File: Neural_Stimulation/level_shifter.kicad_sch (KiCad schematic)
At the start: 4 parts, among them U6 SN74LV1T34DBV, U7 SN74LV1T34DBV, U8 SN74LV1T34DBV, U9 SN74LV1T34DBV

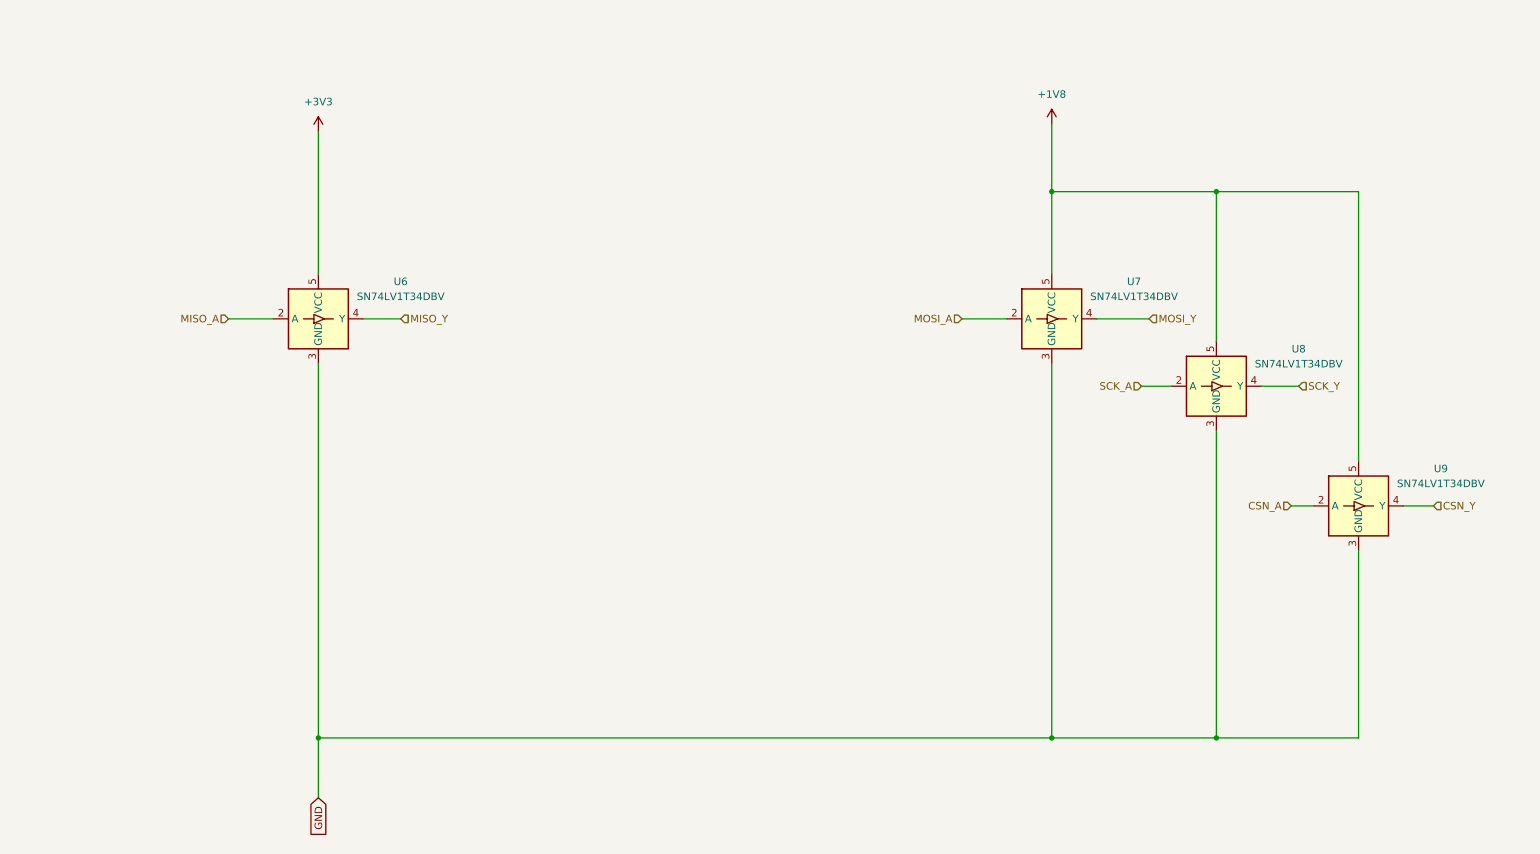
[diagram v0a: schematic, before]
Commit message: Added INT, TRIG, ATEST and RSTN pin circuits
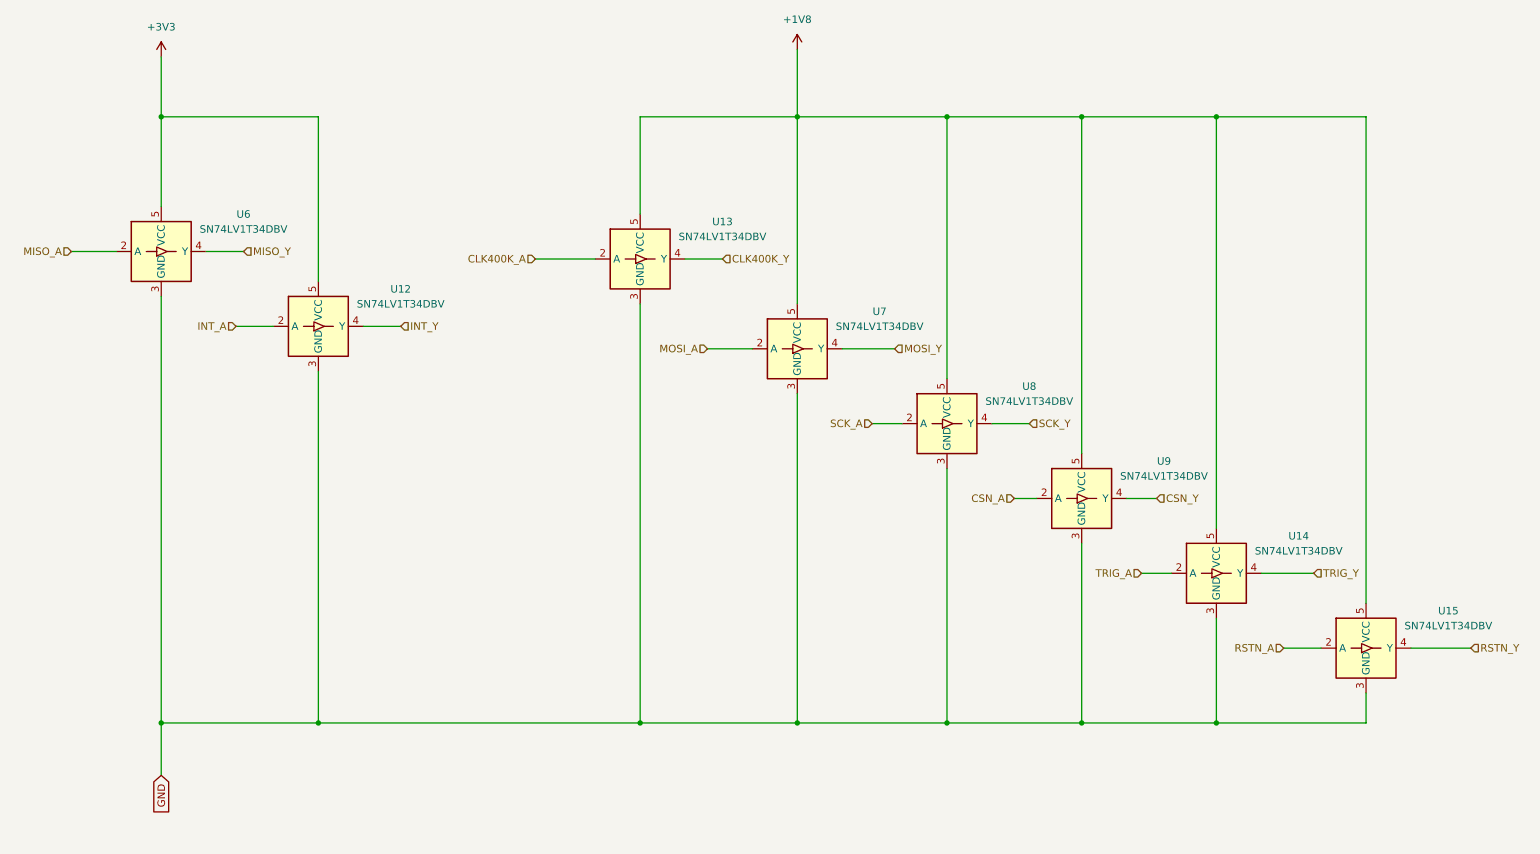
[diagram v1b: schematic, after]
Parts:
- added U12, U13, U14, U15: SN74LV1T34DBV, Package_TO_SOT_SMD:SOT-23-5, symbol Logic_LevelTranslator:SN74LV1T34DBV
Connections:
- net +1V8: now also U13.5 (VCC), U14.5 (VCC), U15.5 (VCC)
- net +3V3: now also U12.5 (VCC)
- net GND: now also U12.3 (GND), U13.3 (GND), U14.3 (GND), U15.3 (GND)
- new net CLK400K_A: U13.2 (A)
- new net CLK400K_Y: U13.4 (Y)
- new net INT_A: U12.2 (A)
- new net INT_Y: U12.4 (Y)
- new net RSTN_A: U15.2 (A)
- new net RSTN_Y: U15.4 (Y)
- new net TRIG_A: U14.2 (A)
- new net TRIG_Y: U14.4 (Y)
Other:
- moved on the sheet: U6, U7, U8, U9
